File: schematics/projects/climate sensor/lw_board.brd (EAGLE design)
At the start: 87.3 x 61 mm, 34 parts, among them J10 J2, J12 J4_FS_2, J5 KF301-5.0, J6 KF301-5.0, Q1 2N3904, Q2 2N3904, Q3 2N3904, Q4 2N3904, Q5 2N3904, Q6 2N3904, U1 GY-SGP30, U2 ESP32 DEVKIT WROOM-32D, U3 PMS7003, U4 BH1750, U5 BME280, U6 MH_Z19B

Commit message: SGP30 sensor works now. I2C bus fully tested.
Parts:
- R7: value 30 -> 5 om, 2W
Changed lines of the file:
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@@
 <drawing>
 <settings>
-<setting alwaysvectorfont="yes"/>
+<setting alwaysvectorfont="no"/>
 <setting verticaltext="up"/>
 </settings>
@@
 <attribute name="R" value="" x="-52.07" y="15.24" size="1.778" layer="27" rot="R270" display="off"/>
 </element>
-<element name="R7" library="my_devices" package="R" value="30" x="66.04" y="46.99" smashed="yes" rot="R270">
+<element name="R7" library="my_devices" package="R" value="5 om, 2W" x="66.04" y="46.99" smashed="yes" rot="R270">
 <attribute name="R" value="" x="-24.13" y="-3.81" size="1.778" layer="27" rot="R270" display="off"/>
 </element>

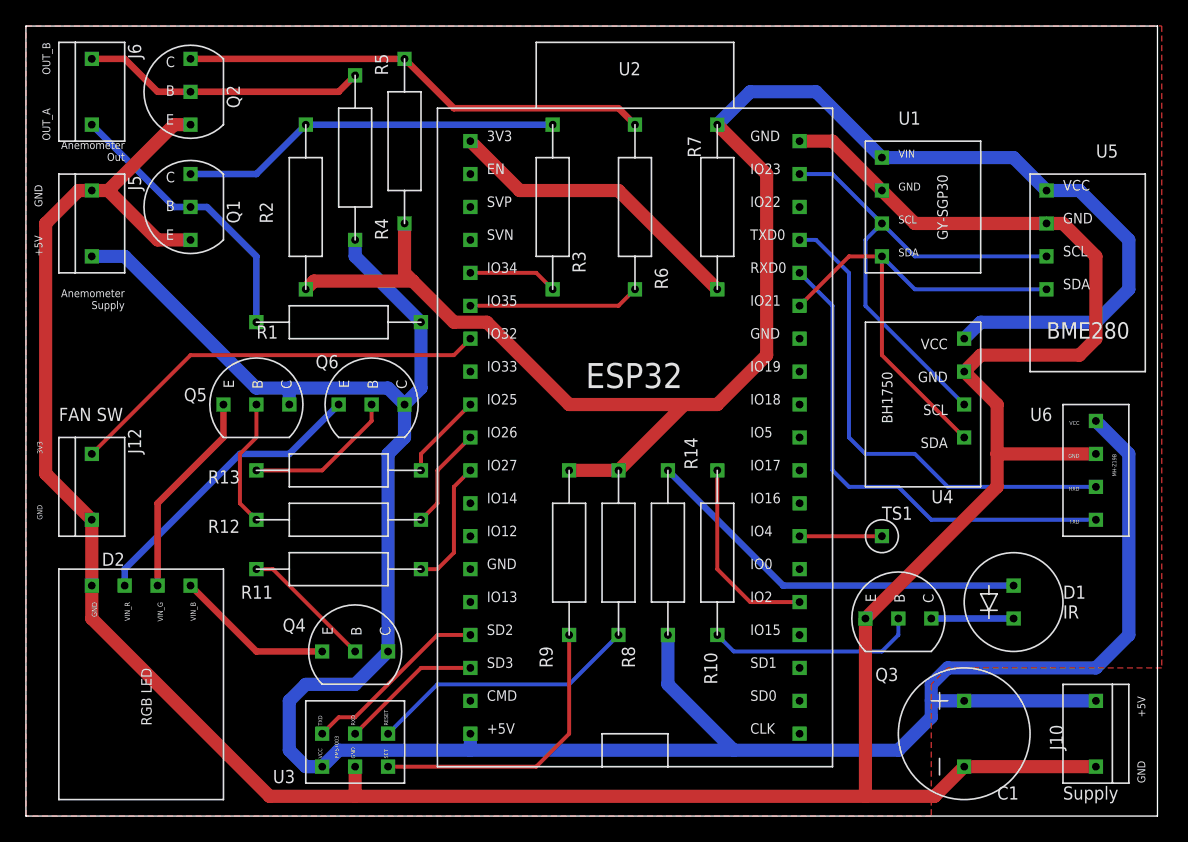
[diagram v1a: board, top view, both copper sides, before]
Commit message: Fixed issues in board.
I received board from jlcpcb

This commit fixed issues in board:
1. drill size increased - it was too small for some components.
2. 'J2' component in library was re-drawed using sizes from datasheet
3. Textes for J2 component was increased in size and moved to bPlace
layer (bottom layer). On top layer not enougth space for it.
4. Increased minimum size for routes.
5. Added 3 holes
6. Re-routed some places - some routes moved to bottom layer.
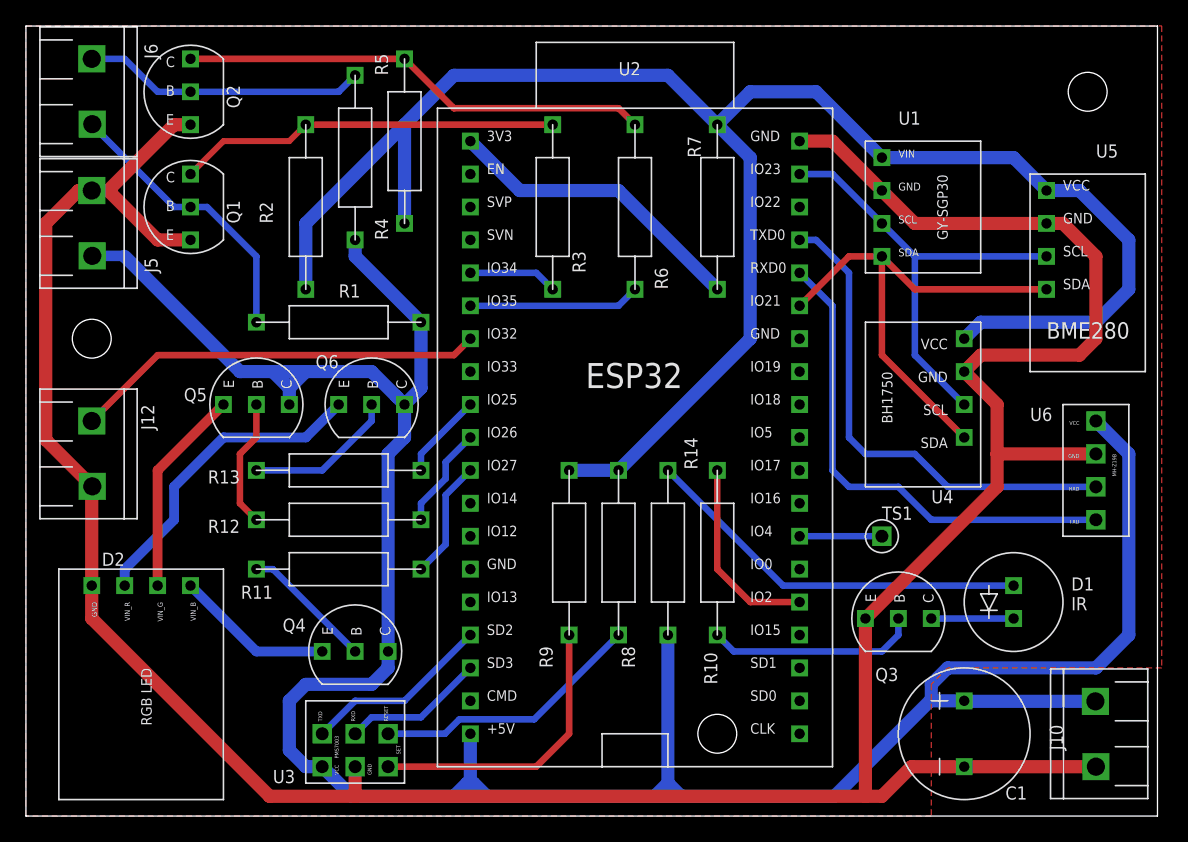
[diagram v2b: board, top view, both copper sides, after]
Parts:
- Q1, Q2, Q3, Q4, Q5, Q6: device my_devices:TRANSISTOR_NPN -> my_devices:TRANSISTOR
- moved J12 2.54 mm to (17.8, 27.9)
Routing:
- net +5V: track 191.6 -> 208.3 mm
- net 3V3: track 132.0 -> 142.1 mm
- net I2C_SCL: track 39.3 -> 34.7 mm
- net N$3: track 23.0 -> 24.5 mm
- net N$11: track 32.9 -> 31.8 mm
- net GPIO_RGB_B: track 9.94 -> 9.20 mm
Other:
- board text added: "A"
- board text added: "AN_OUT"
- board text added: "AN_SUPPLY"
- board text added: "B"
- board text added: "SUPPLY"
- board text removed: "Anemometer Out"
- board text removed: "Anemometer Supply"
- board text removed: "OUT_A"
- board text removed: "OUT_B"
- board text removed: "Supply"
